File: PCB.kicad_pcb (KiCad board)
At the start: 4 copper layers, 200 x 150 mm, 518 parts, among them J1 PASSIVE_CHANNELS, J10 USB_RASPBERRY, J11 USB_ARDUINO, J12 100W_ch+, J13 100W_ch-, J14 100W_sense, J15 PowerMosGate, J16 PowerMosDrain, J17 PowerMosSource, J2 PASSIVE_CHANNELS, J3 PASSIVE_CHANNELS, J4 12V+, J5 12V-, J6 5V_PI, J7 5V_PI, J8 ACTIVE_5W_CHANNELS, J9 5V_PI, Q1 BT137-600, Q10 IRLB3813PBF, Q11 IRLB3813PBF, Q12 IRLB3813PbF, Q13 IRLB3813PbF, Q14 IRLB3813PbF, Q15 IRLB3813PbF, Q16 IRLB3813PbF, Q17 IRLB3813PbF, Q2 IRLB3813PbF, Q3 IRLB3813PbF, Q4 IRLB3813PBF, Q5 IRLB3813PBF, Q6 IRLB3813PBF, Q7 IRLB3813PBF, Q8 IRLB3813PBF, Q9 IRLB3813PBF, SW1 RESET_SW, T1+1 TestPoint, T1+2 TestPoint, T1+3 TestPoint, T1+4 TestPoint, T1+5 TestPoint, T1+6 TestPoint, T1+7 TestPoint, T1+8 TestPoint, T1-1 TestPoint, T1-2 TestPoint, T1-3 TestPoint, T1-4 TestPoint, T1-5 TestPoint, T1-6 TestPoint, T1-7 TestPoint, T1-8 TestPoint, T2+1 TestPoint, T2+2 TestPoint, T2+3 TestPoint, T2+4 TestPoint, T2+5 TestPoint, T2+6 TestPoint, T2+7 TestPoint, T2+8 TestPoint, T2-1 TestPoint, T2-2 TestPoint, T2-3 TestPoint, T2-4 TestPoint, T2-5 TestPoint, T2-6 TestPoint, T2-7 TestPoint, T2-8 TestPoint, U1 LM431ACM3_NOPB, U10 INA250A4PW, U11 INA250A4PW, U12 INA250A4PW, U13 ADC124S021CIMM_NOPB, U14 INA250A4PW, U15 INA250A4PW, U16 INA250A4PW, U17 INA250A4PW, U18 ADC124S021CIMM_NOPB, U19 INA250A4PW, U2 LM1117-ADJ, U20 INA250A4PW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

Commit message: Placement Charge active 100w et filtres PWM
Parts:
- moved J14 308.1 mm to (410.0, 130.0)
- moved TPVA1 289.9 mm to (50.9, 185.9)
- moved TPVA2 289.9 mm to (54.0, 185.9)
- moved C2 236.8 mm to (40.0, 128.0)
- moved R4 233.9 mm to (28.9, 131.1)
- moved R5 233.9 mm to (34.5, 131.1)
- moved C6 222.4 mm to (92.5, 131.0)
- moved C3 222.1 mm to (89.0, 131.0)
- moved R86 221.4 mm to (354.0, 105.0), turned to 270 degrees
- moved R85 218.7 mm to (354.0, 102.0), turned to 270 degrees
- moved C4 213.2 mm to (55.8, 109.9)
- moved SW1 213.2 mm to (41.8, 110.4)
- moved R84 180.2 mm to (368.0, 104.0), turned to 270 degrees
- moved R83 180.2 mm to (368.0, 101.0), turned to 270 degrees
- moved C68 180.0 mm to (362.0, 107.0)
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
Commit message: Small modifications
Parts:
- moved R140 2.00 mm to (254.2, 123.0)
- moved R141 2.00 mm to (254.2, 126.2)
- moved R144 2.00 mm to (254.6, 118.9)
- moved TPOA1 0.75 mm to (366.2, 159.0)
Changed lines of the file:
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@@
   )
   (setup
-    (last_trace_width 1.6)
+    (last_trace_width 0.2)
     (user_trace_width 1.6)
     (trace_clearance 0.2)
@@
   )
   (module TestPoint:TestPoint_Pad_1.0x1.0mm (layer F.Cu)
-    (at 366.25 158.25)
+    (at 366.25 159)
     (descr "SMD rectangular pad as test Point, square 1.0mm side length")
     (tags "test point SMD pad rectangle square")
@@
   )
   (module Resistor_SMD:R_0805_2012Metric (layer F.Cu)
-    (at 254.23 125 270)
+    (at 254.23 123 270)
     (descr "Resistor SMD 0805 (2012 Metric), square (rectangular) end terminal, IPC_7351 nominal, (Body size source: https://docs.google.com/spreadsheets/d/1BsfQQcO9C6DZCsRaXUlFlo91Tg2WpOkGARC1WS5S8t0/edit?usp=sharing), generated with kicad-footprint-generator")
     (tags resistor)
@@
   )
   (module Resistor_SMD:R_0805_2012Metric (layer F.Cu)
-    (at 254.23 128.18 270)
+    (at 254.23 126.18 270)
     (descr "Resistor SMD 0805 (2012 Metric), square (rectangular) end terminal, IPC_7351 nominal, (Body size source: https://docs.google.com/spreadsheets/d/1BsfQQcO9C6DZCsRaXUlFlo91Tg2WpOkGARC1WS5S8t0/edit?usp=sharing), generated with kicad-footprint-generator")
     (tags resistor)
@@
   )
   (module Resistor_SMD:R_0805_2012Metric (layer F.Cu)
-    (at 254.59 120.94 90)
+    (at 254.59 118.94 90)
     (descr "Resistor SMD 0805 (2012 Metric), square (rectangular) end terminal, IPC_7351 nominal, (Body size source: https://docs.google.com/spreadsheets/d/1BsfQQcO9C6DZCsRaXUlFlo91Tg2WpOkGARC1WS5S8t0/edit?usp=sharing), generated with kicad-footprint-generator")
     (tags resistor)

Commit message: Defi releve!
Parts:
- removed J17: PowerMosSource, PCB:30ATerminal
- D1: footprint Package_TO_SOT_SMD:TO-277A -> PCB:TO-277A
- moved SW1 169.3 mm to (210.5, 125.0)
- moved R4 140.6 mm to (168.5, 147.6), turned to 270 degrees
- moved R5 132.0 mm to (165.5, 147.4), turned to 90 degrees
- moved C2 127.5 mm to (167.0, 139.0), turned to 180 degrees
- moved C7 127.4 mm to (167.1, 143.0), turned to 180 degrees
- moved U2 125.6 mm to (172.2, 145.9), turned to 90 degrees
- moved C4 112.4 mm to (162.5, 145.0), turned to 90 degrees
- moved D18 107.0 mm to (306.0, 143.0), turned to 90 degrees
- moved U31 101.1 mm to (298.5, 166.8), turned to 270 degrees
- moved C70 100.1 mm to (295.0, 165.5), turned to 90 degrees
- moved U30 98.7 mm to (291.5, 166.8), turned to 270 degrees
- moved J14 97.3 mm to (314.0, 146.0), turned to 270 degrees
- moved C69 97.2 mm to (288.0, 165.5), turned to 90 degrees
- moved J11 96.0 mm to (128.9, 93.5)
- moved J10 96.0 mm to (128.8, 111.1)
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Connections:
- J10 pad 1: Net-(J10-Pad1) -> (no net)
- J11 pad 1: Net-(J11-Pad1) -> (no net)
- S2 pad 1: Net-(S2-Pad1) -> (no net)
- S3 pad 1: Net-(S3-Pad1) -> (no net)
- S4 pad 1: Net-(S4-Pad1) -> (no net)
- S5 pad 1: Net-(S5-Pad1) -> (no net)
- S6 pad 1: Net-(S6-Pad1) -> (no net)
- XA1 pad 3V3: Net-(XA1-Pad3V3) -> (no net)
- XA1 pad 5V2: Net-(XA1-Pad5V2) -> (no net)
- XA1 pad AREF: Net-(XA1-PadAREF) -> (no net)
- XA1 pad D0: Net-(XA1-PadD0) -> (no net)
- XA1 pad D1: Net-(XA1-PadD1) -> (no net)
- XA1 pad D12: Net-(XA1-PadD12) -> (no net)
- XA1 pad D13: Net-(XA1-PadD13) -> (no net)
- XA1 pad D14: Net-(XA1-PadD14) -> (no net)
- XA1 pad D15: Net-(XA1-PadD15) -> (no net)
- XA1 pad D16: Net-(XA1-PadD16) -> (no net)
- XA1 pad D17: Net-(XA1-PadD17) -> (no net)
- XA1 pad D18: Net-(XA1-PadD18) -> (no net)
- XA1 pad D19: Net-(XA1-PadD19) -> (no net)
- XA1 pad D20: Net-(XA1-PadD20) -> (no net)
- XA1 pad D21: Net-(XA1-PadD21) -> (no net)
- XA1 pad D35: Net-(XA1-PadD35) -> (no net)
- XA1 pad D36: Net-(XA1-PadD36) -> (no net)
- XA1 pad D37: Net-(XA1-PadD37) -> (no net)
- XA1 pad D38: Net-(XA1-PadD38) -> (no net)
- XA1 pad D39: Net-(XA1-PadD39) -> (no net)
- XA1 pad D4: Net-(XA1-PadD4) -> (no net)
- XA1 pad D40: Net-(XA1-PadD40) -> (no net)
- XA1 pad D41: Net-(XA1-PadD41) -> (no net)
- XA1 pad D42: Net-(XA1-PadD42) -> (no net)
- XA1 pad D43: Net-(XA1-PadD43) -> (no net)
- XA1 pad D44: Net-(XA1-PadD44) -> (no net)
- XA1 pad D45: Net-(XA1-PadD45) -> (no net)
- XA1 pad GND4: Net-(XA1-PadGND4) -> (no net)
- XA1 pad IORF: Net-(XA1-PadIORF) -> (no net)
- XA1 pad RST2: Net-(XA1-PadRST2) -> (no net)
- XA1 pad SCL: Net-(XA1-PadSCL) -> (no net)
- XA1 pad SDA: Net-(XA1-PadSDA) -> (no net)
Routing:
- added copper zone on B.Cu, net /+12V
- added copper zone on F.Cu, net /+12V
- added copper zone on F.Cu, net /VinActif100W
- added copper zone on F.Cu, net /VoutActif100W

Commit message: Test placements
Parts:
- moved J13 72.4 mm to (382.5, 179.0), turned to 90 degrees
- moved J15 66.8 mm to (368.0, 175.2), turned to 0 degrees
- moved J16 51.3 mm to (358.2, 179.0), turned to 90 degrees
- moved TPV-1 33.4 mm to (379.6, 189.7), turned to 0 degrees
- moved R127 30.7 mm to (375.0, 191.5), turned to 270 degrees
- moved TPOA1 30.5 mm to (368.6, 194.7), turned to 0 degrees
- moved TPVAD1 29.6 mm to (356.2, 187.8), turned to 0 degrees
- moved C101 28.9 mm to (373.1, 191.2), turned to 90 degrees
- moved TPV+1 28.9 mm to (358.9, 194.4), turned to 0 degrees
- moved R131 26.9 mm to (374.9, 187.9), turned to 90 degrees
- moved R133 25.2 mm to (373.1, 187.9), turned to 270 degrees
- moved R129 24.5 mm to (363.6, 191.4), turned to 270 degrees
- moved C103 24.3 mm to (362.1, 191.4), turned to 90 degrees
- moved J12 24.2 mm to (310.2, 149.0)
- moved R128 24.1 mm to (359.9, 191.2), turned to 0 degrees
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
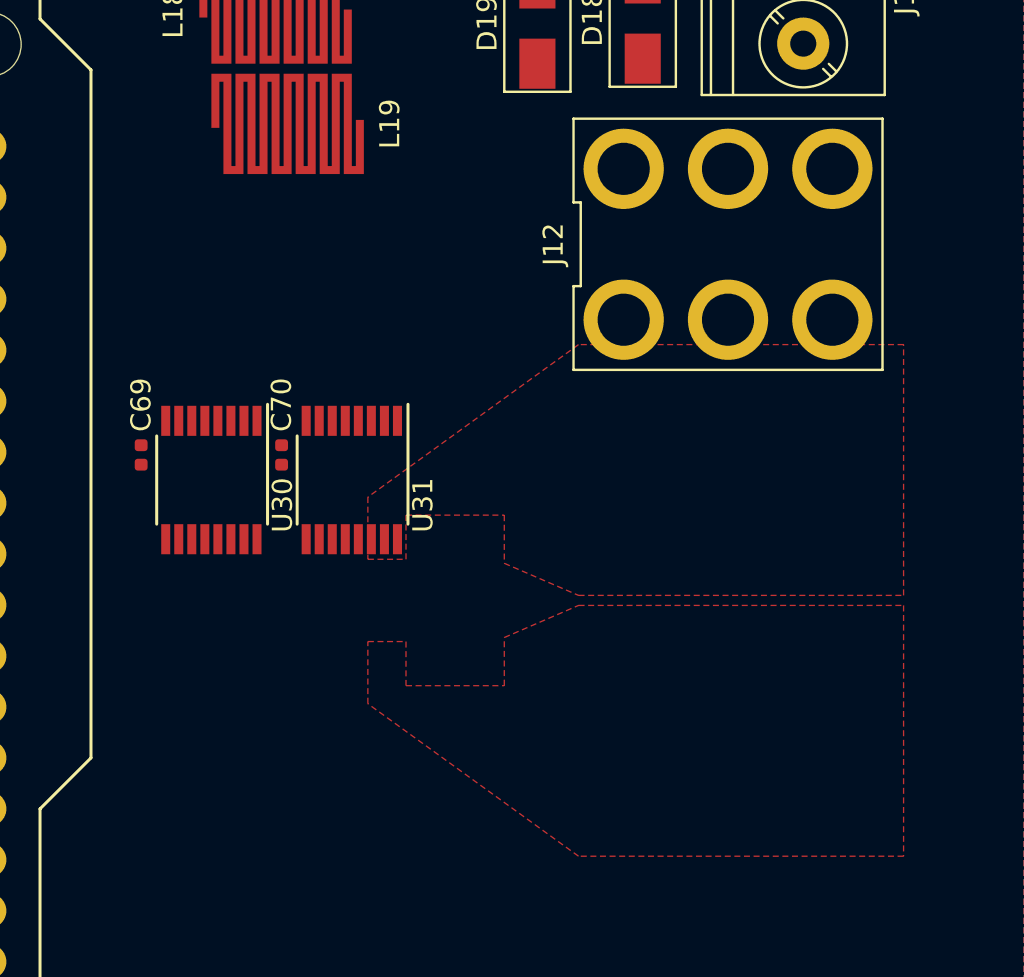
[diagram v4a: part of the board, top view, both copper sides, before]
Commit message: Placement current sensors avec pads
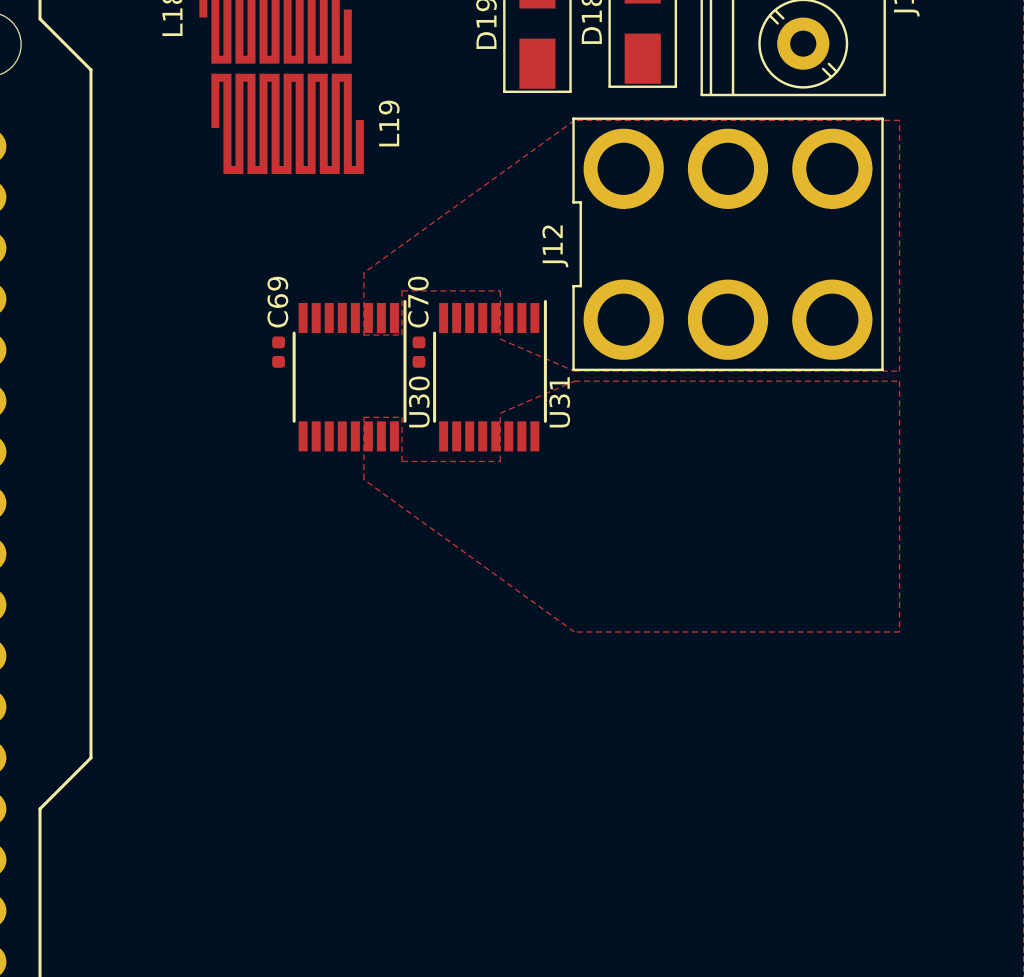
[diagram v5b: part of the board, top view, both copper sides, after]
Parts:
- moved C69 8.56 mm to (287.9, 154.4)
- moved C70 8.56 mm to (294.9, 154.4)
- moved U30 8.56 mm to (291.4, 155.6)
- moved U31 8.56 mm to (298.4, 155.6)
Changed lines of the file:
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@@
   )
   (setup
-    (last_trace_width 13)
+    (last_trace_width 0.2)
     (user_trace_width 0.2)
     (user_trace_width 0.5)
@@
   )
   (module Capacitor_SMD:C_0402_1005Metric (layer F.Cu)
-    (at 281 159.5 90)
+    (at 287.85 154.375 90)
     (descr "Capacitor SMD 0402 (1005 Metric), square (rectangular) end terminal, IPC_7351 nominal, (Body size source: http://www.tortai-tech.com/upload/download/2011102023233369053.pdf), generated with kicad-footprint-generator")
     (tags capacitor)
@@
   )
   (module Capacitor_SMD:C_0402_1005Metric (layer F.Cu)
-    (at 288 159.5 90)
+    (at 294.85 154.375 90)
     (descr "Capacitor SMD 0402 (1005 Metric), square (rectangular) end terminal, IPC_7351 nominal, (Body size source: http://www.tortai-tech.com/upload/download/2011102023233369053.pdf), generated with kicad-footprint-generator")
     (tags capacitor)
@@
   )
   (module Package_SO:TSSOP-16_4.4x5mm_P0.65mm (layer F.Cu)
-    (at 284.5 160.75 270)
+    (at 291.35 155.625 270)
     (descr "16-Lead Plastic Thin Shrink Small Outline (ST)-4.4 mm Body [TSSOP] (see Microchip Packaging Specification 00000049BS.pdf)")
     (tags "SSOP 0.65")
@@
   )
   (module Package_SO:TSSOP-16_4.4x5mm_P0.65mm (layer F.Cu)
-    (at 291.5 160.75 270)
+    (at 298.35 155.625 270)
     (descr "16-Lead Plastic Thin Shrink Small Outline (ST)-4.4 mm Body [TSSOP] (see Microchip Packaging Specification 00000049BS.pdf)")
     (tags "SSOP 0.65")
@@
     (polygon
       (pts
-        (xy 319 179.5) (xy 302.8 179.5) (xy 292.3 171.9) (xy 292.3 168.8) (xy 294.2 168.8)
-        (xy 294.2 171) (xy 299.1 171) (xy 299.1 168.6) (xy 302.8 167) (xy 319 167)
+        (xy 318.8 168.325) (xy 302.6 168.325) (xy 292.1 160.725) (xy 292.1 157.625) (xy 294 157.625)
+        (xy 294 159.825) (xy 298.9 159.825) (xy 298.9 157.425) (xy 302.6 155.825) (xy 318.8 155.825)
       )
     )
@@
     (polygon
       (pts
-        (xy 319 154) (xy 302.8 154) (xy 292.3 161.6) (xy 292.3 164.7) (xy 294.2 164.7)
-        (xy 294.2 162.5) (xy 299.1 162.5) (xy 299.1 164.9) (xy 302.8 166.5) (xy 319 166.5)
+        (xy 318.8 142.825) (xy 302.6 142.825) (xy 292.1 150.425) (xy 292.1 153.525) (xy 294 153.525)
+        (xy 294 151.325) (xy 298.9 151.325) (xy 298.9 153.725) (xy 302.6 155.325) (xy 318.8 155.325)
       )
     )
